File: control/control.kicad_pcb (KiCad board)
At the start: 2 copper layers, 100 x 50 mm, 58 parts, among them J1 Conn_01x06_Male, J2 Conn_01x03_Male, J3 footswitch, Q1 TD9944, Q2 TD9944, Q3 TD9944, Q4 TD9944, SW1 SW_SPST_X3, U1 Teensy_LC, U2 MCP3208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

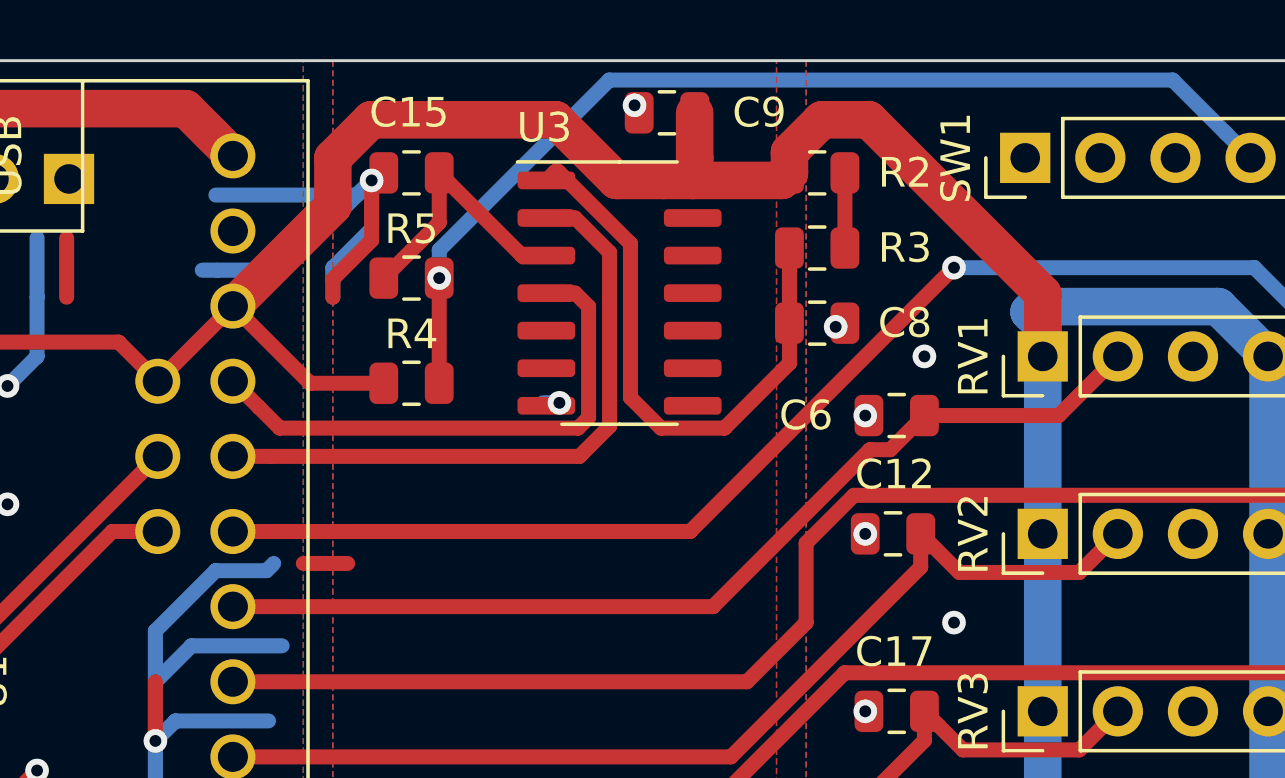
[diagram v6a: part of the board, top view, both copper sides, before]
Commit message: Ajout de documentation dans les schématiques
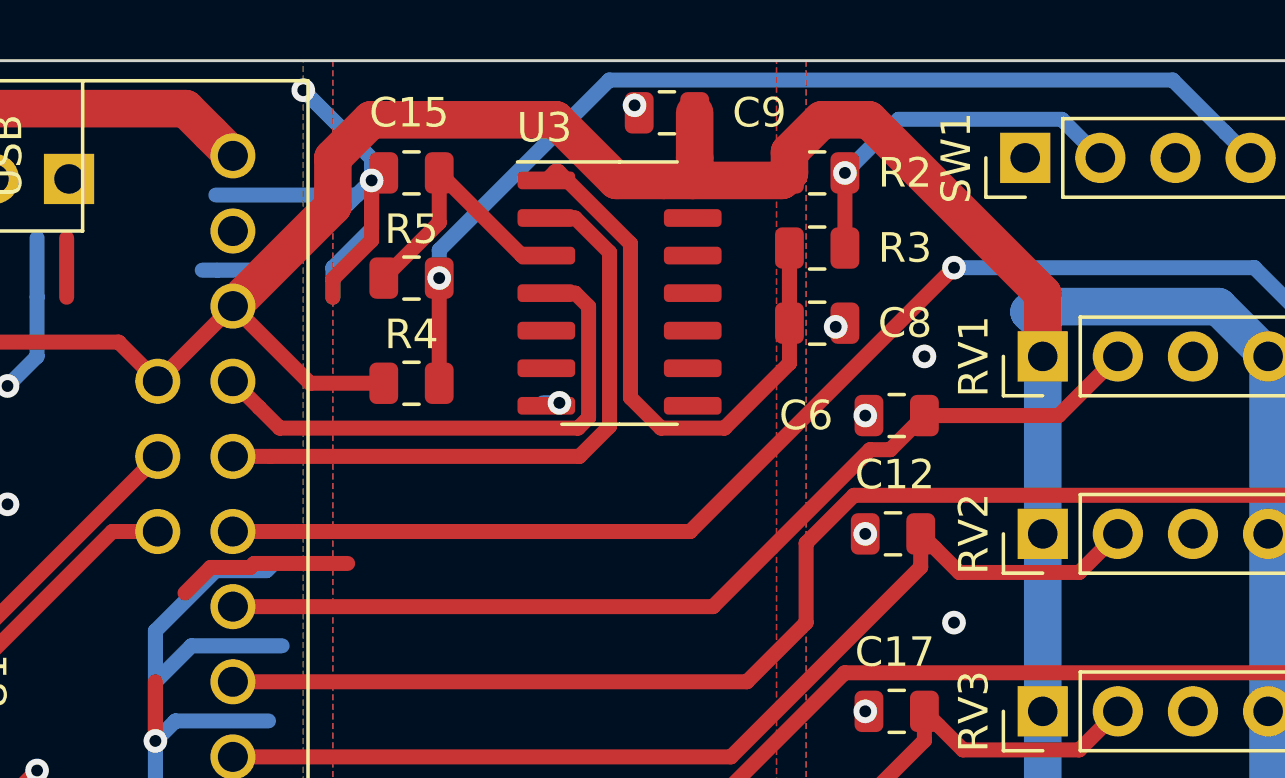
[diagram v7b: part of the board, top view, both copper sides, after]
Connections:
- net Net-(J3-Pad5) renamed /MCU/FS_RS232_RX
- net Net-(J3-Pad6) renamed /MCU/FS_RS232_TX
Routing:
- net Net-(R2-Pad2): track 2.54 -> 12.5 mm, vias 0 -> 1
- net GNDD: track 232.2 -> 240.6 mm, vias 54 -> 55

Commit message: Ajout des gerber pour control et footswitch.
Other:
- board text added: "+ - overdrive/comp/mute/pad"
- board text added: "- + octaver/delay/reverb/clip"
- board text added: "12V"
- board text added: "5V"
- board text added: "EQ high mid/high"
- board text added: "EQ low/low mid"
- board text added: "FAN"
- board text added: "FS"
- board text added: "G"
- board text added: "POWER"
- board text added: "RX"
- board text added: "TX"
- board text added: "comp ratio/threshold"
- board text added: "contour/presence"
- board text added: "delay/reverb"
- board text added: "mute/delay tap"
- board text added: "octaver down/up"
- board text added: "overdrive gain/tone"
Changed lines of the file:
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@@
   (general
     (thickness 1.6)
-    (drawings 4)
+    (drawings 28)
     (tracks 652)
     (zones 0)
@@
   )
   (setup
-    (last_trace_width 0.508)
+    (last_trace_width 0.25)
     (user_trace_width 0.254)
     (user_trace_width 0.381)
@@
     (pcbplotparams
       (layerselection 0x010fc_ffffffff)
-      (usegerberextensions false)
+      (usegerberextensions true)
       (usegerberattributes false)
       (usegerberadvancedattributes false)
@@
       (drillshape 0)
       (scaleselection 1)
-      (outputdirectory "/home/marc-antoine/Bureau/test/"))
+      (outputdirectory "gerber"))
   )
   (net 0 "")
@@
     (tags capacitor)
     (attr smd)
-    (fp_text reference C27 (at 2.9375 0 180) (layer F.SilkS)
+    (fp_text reference C27 (at 2.4375 0 180) (layer F.SilkS)
       (effects (font (size 1 1) (thickness 0.15)))
     )
@@
     (tags capacitor)
     (attr smd)
-    (fp_text reference C23 (at 2.9375 0 180) (layer F.SilkS)
+    (fp_text reference C23 (at 0.9375 -2.5 180) (layer F.SilkS)
       (effects (font (size 1 1) (thickness 0.15)))
     )
@@
     (tags capacitor)
     (attr smd)
-    (fp_text reference C25 (at 1.9375 2 180) (layer F.SilkS)
+    (fp_text reference C25 (at 1.9375 1.5 180) (layer F.SilkS)
       (effects (font (size 1 1) (thickness 0.15)))
     )
@@
     (tags capacitor)
     (attr smd)
-    (fp_text reference C26 (at 2.9375 -1 90) (layer F.SilkS)
+    (fp_text reference C26 (at 2.4375 0 90) (layer F.SilkS)
       (effects (font (size 1 1) (thickness 0.15)))
     )
@@
     (descr "CP, Radial series, Radial, pin pitch=5.00mm, , diameter=10mm, Electrolytic Capacitor")
     (tags "CP Radial series Radial pin pitch 5.00mm  diameter 10mm Electrolytic Capacitor")
-    (fp_text reference C1 (at 5 -6) (layer F.SilkS)
+    (fp_text reference C1 (at -3.5 0 90) (layer F.SilkS)
       (effects (font (size 1 1) (thickness 0.15)))
     )
@@
     (descr "CP, Radial series, Radial, pin pitch=5.00mm, , diameter=10mm, Electrolytic Capacitor")
     (tags "CP Radial series Radial pin pitch 5.00mm  diameter 10mm Electrolytic Capacitor")
-    (fp_text reference C2 (at 2.5 -6.25) (layer F.SilkS)
+    (fp_text reference C2 (at -3.5 0 90) (layer F.SilkS)
       (effects (font (size 1 1) (thickness 0.15)))
     )
@@
     )
   )
+  (gr_text "mute/delay tap" (at 96 21) (layer F.SilkS)
+    (effects (font (size 1 1) (thickness 0.15)))
+  )
+  (gr_text contour/presence (at 96 27.5) (layer F.SilkS)
+    (effects (font (size 1 1) (thickness 0.15)))
+  )
+  (gr_text "EQ low/low mid" (at 96 33.5) (layer F.SilkS)
+    (effects (font (size 1 1) (thickness 0.15)))
+  )
+  (gr_text "EQ high mid/high" (at 96 39.5) (layer F.SilkS)
+    (effects (font (size 1 1) (thickness 0.15)))
+  )
+  (gr_text "comp ratio/threshold" (at 96 45.5) (layer F.SilkS)
+    (effects (font (size 1 1) (thickness 0.15)))
+  )
+  (gr_text "overdrive gain/tone" (at 96 51.5) (layer F.SilkS)
+    (effects (font (size 1 1) (thickness 0.15)))
+  )
+  (gr_text "octaver down/up" (at 96 57.5) (layer F.SilkS)
+    (effects (font (size 1 1) (thickness 0.15)))
+  )
+  (gr_text delay/reverb (at 96.5 63.5) (layer F.SilkS)
+    (effects (font (size 1 1) (thickness 0.15)))
+  )
+  (gr_text "- + octaver/delay/reverb/clip" (at 61.5 63.5) (layer F.SilkS)
+    (effects (font (size 1 1) (thickness 0.15)))
+  )
+  (gr_text "+ - overdrive/comp/mute/pad" (at 35 63.5) (layer F.SilkS)
+    (effects (font (size 1 1) (thickness 0.15)))
+  )
+  (gr_text TX (at 38 22 90) (layer F.SilkS)
+    (effects (font (size 1 1) (thickness 0.15)))
+  )
+  (gr_text RX (at 35 22 90) (layer F.SilkS)
+    (effects (font (size 1 1) (thickness 0.15)))
+  )
+  (gr_text 12V (at 32.5 22 90) (layer F.SilkS)
+    (effects (font (size 1 1) (thickness 0.15)))
+  )
+  (gr_text G (at 27.5 21.5 90) (layer F.SilkS)
+    (effects (font (size 1 1) (thickness 0.15)))
+  )
+  (gr_text G (at 25 21.5 90) (layer F.SilkS)
+    (effects (font (size 1 1) (thickness 0.15)))
+  )
+  (gr_text G (at 34.5 37 90) (layer F.SilkS)
+    (effects (font (size 1 1) (thickness 0.15)))
+  )
+  (gr_text G (at 32 37 90) (layer F.SilkS)
+    (effects (font (size 1 1) (thickness 0.15)))
+  )
+  (gr_text G (at 29.5 37 90) (layer F.SilkS)
+    (effects (font (size 1 1) (thickness 0.15)))
+  )
+  (gr_text 5V (at 30 22 90) (layer F.SilkS)
+    (effects (font (size 1 1) (thickness 0.15)))
+  )
+  (gr_text FS (at 41 19) (layer F.SilkS)
+    (effects (font (size 1 1) (thickness 0.15)))
+  )
+  (gr_text POWER (at 23.5 37) (layer F.SilkS)
+    (effects (font (size 1 1) (thickness 0.15)))
+  )
+  (gr_text FAN (at 27 43 90) (layer F.SilkS)
+    (effects (font (size 1 1) (thickness 0.15)))
+  )
+  (gr_text 12V (at 24.5 43 90) (layer F.SilkS)
+    (effects (font (size 1 1) (thickness 0.15)))
+  )
+  (gr_text 5V (at 22 43 90) (layer F.SilkS)
+    (effects (font (size 1 1) (thickness 0.15)))
+  )
   (gr_line (start 115 15) (end 15 15) (layer Edge.Cuts) (width 0.1))
